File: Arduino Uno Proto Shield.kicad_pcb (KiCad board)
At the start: 2 copper layers, 68.6 x 53.3 mm, 423 parts, among them J1 CONN_POWER, J10 A0, J11 A1, J12 A2, J13 A3, J14 A5, J15 A6, J16 SCL, J17 SDA, J18 AREF, J19 GND, J2 CONN_ANALOG_IN, J20 13, J21 12, J22 (PWM) 11, J23 (PWM) 10, J24 (PWM) 9, J25 8, J26 7, J27 (PWM) 6, J28 (PWM) 5, J29 4, J3 IOREF, J30 (PWM) 3, J31 2, J32 (TX) 1, J33 (RX) 0, J34 CONN_DIGITAL_8-13, J35 CONN_DIGITAL_0-7, J4 RESET, J5 3.3V, J6 5V, J7 GND, J8 GND, J9 VIN

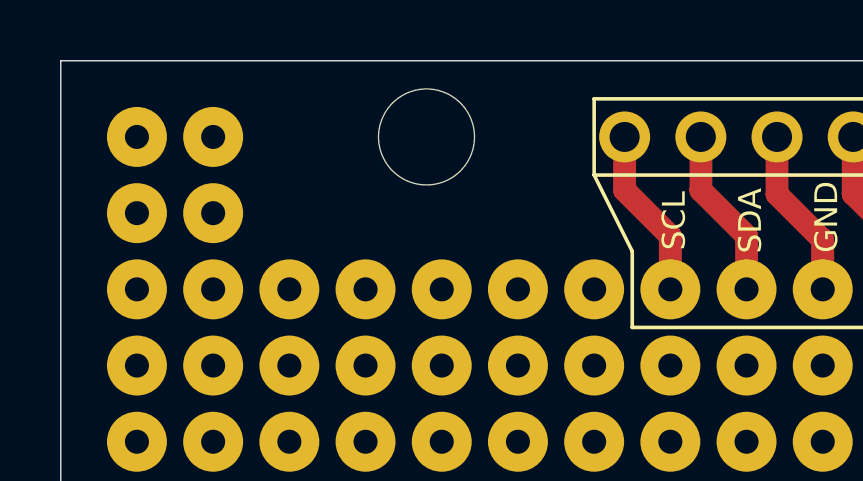
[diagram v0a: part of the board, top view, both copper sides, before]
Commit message: Fix mounting hole placement
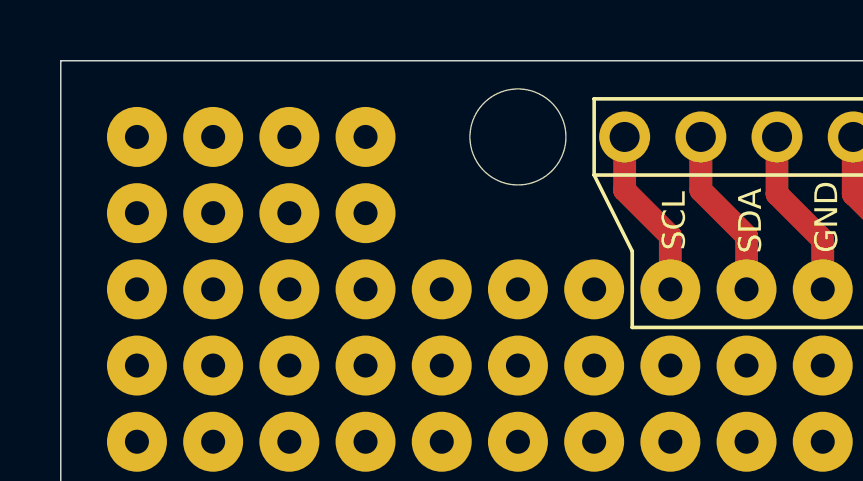
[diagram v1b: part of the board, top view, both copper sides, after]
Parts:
- added REF**: SolderWirePad_1x01_Drill0.8mm, Connector_Wire:SolderWirePad_1x01_Drill0.8mm, F.Cu at (111.8, 76.2)
- added REF**: SolderWirePad_1x01_Drill0.8mm, Connector_Wire:SolderWirePad_1x01_Drill0.8mm, F.Cu at (111.8, 78.7)
- added REF**: SolderWirePad_1x01_Drill0.8mm, Connector_Wire:SolderWirePad_1x01_Drill0.8mm, F.Cu at (109.2, 76.2)
- added REF**: SolderWirePad_1x01_Drill0.8mm, Connector_Wire:SolderWirePad_1x01_Drill0.8mm, F.Cu at (109.2, 78.7)
- moved REF** 3.05 mm to (116.8, 76.2)
